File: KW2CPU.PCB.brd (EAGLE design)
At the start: 50 x 30 mm, 57 parts, among them IC1 AT45DB161D8S1

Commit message: Rotated board
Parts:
- added LED1: (no value), adafruit:CHIPLED_0805
- added SJ1: (no value), jumper:SJ
- moved U$4 40.8 mm to (-3.79, 6.27), turned to 180 degrees
- moved U$5 38.3 mm to (1.16, -13.1), turned to 180 degrees
- moved U$6 35.1 mm to (33.0, -0.76), turned to 270 degrees
- moved R2 33.9 mm to (27.7, -12.2), turned to 90 degrees
- moved U$12 32.9 mm to (31.8, -1.01)
- moved C$16 32.7 mm to (0.12, -5.87), turned to 180 degrees
- moved C$18 31.2 mm to (0.14, -3.28), turned to 180 degrees
- moved C$15 31.1 mm to (0.14, 2.07), turned to 180 degrees
- moved L$17 31.0 mm to (0.58, -4.54), turned to 90 degrees
- moved R3 30.9 mm to (22.9, -14.0), turned to 0 degrees
- moved C$13 30.7 mm to (0.14, -0.83), turned to 180 degrees
- moved R$19 30.0 mm to (2.33, -7.61), turned to 270 degrees
- moved L$14 29.9 mm to (0.58, 0.50), turned to 90 degrees
- moved IC2 29.6 mm to (27.1, 8.89), turned to 270 degrees
- moved C$20 29.3 mm to (2.09, -6.33), turned to 0 degrees
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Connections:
- net GND: now also R$23.P$2
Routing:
- net N$22: track 37.7 -> 6.80 mm, vias 1 -> 0
- net N$40: track 38.2 -> 54.4 mm
- net N$13: track 33.1 -> 46.6 mm
- net N$41: track 33.6 -> 44.4 mm
- net N$44: track 34.4 -> 45.2 mm
- net N$11: track 40.0 -> 50.1 mm
- net N$43: track 31.8 -> 40.2 mm
- net +3V3: track 65.0 -> 56.7 mm, vias 10 -> 12
- net N$42: track 38.6 -> 46.7 mm
- net N$10: track 34.5 -> 41.9 mm
- net N$12: track 38.9 -> 45.1 mm
- net N$14: track 36.5 -> 37.2 mm
- net GND: vias 83 -> 84

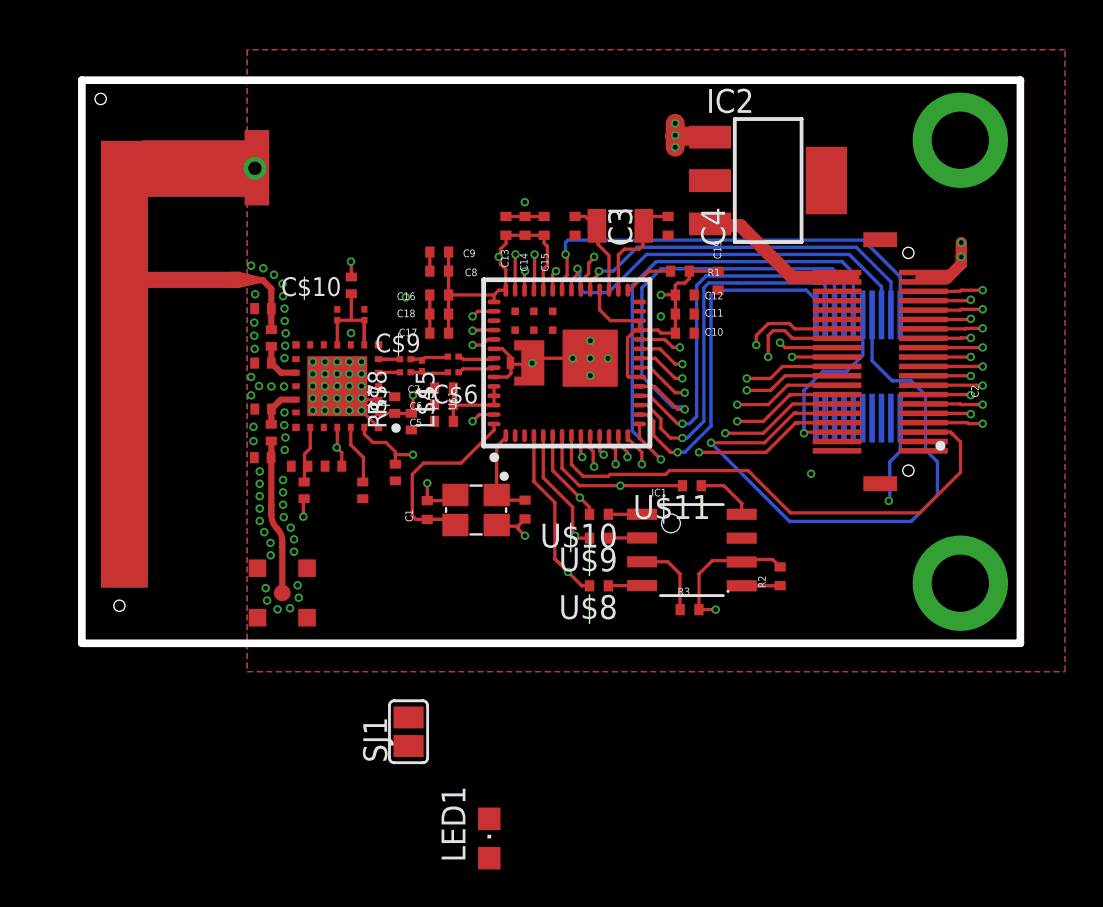
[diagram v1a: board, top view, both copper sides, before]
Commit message: Schematic fix
Almost done fixing schematic
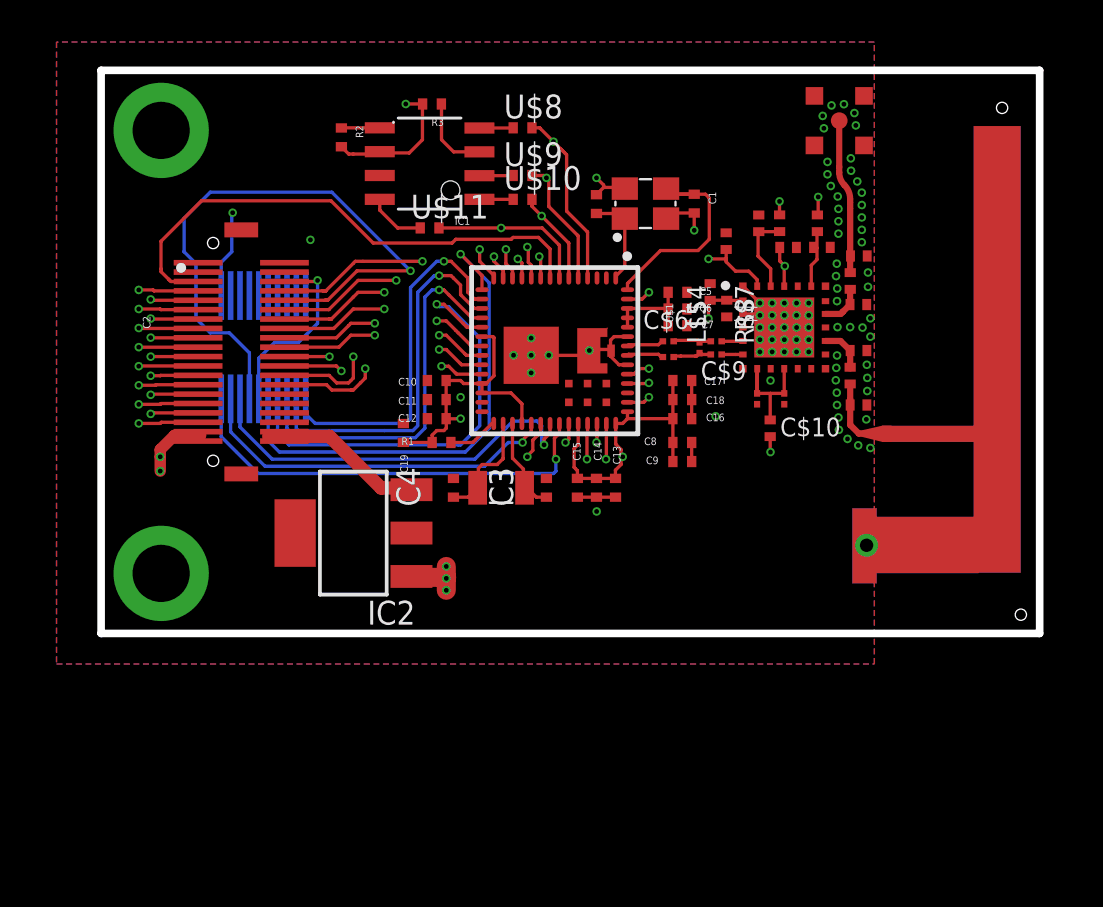
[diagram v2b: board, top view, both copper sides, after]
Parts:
- removed LED1: (no value), adafruit:CHIPLED_0805
- removed SJ1: (no value), jumper:SJ
- added R$2: (no value), GW-devices:RFMD0402
- moved U$4 41.8 mm to (35.8, -7.27), turned to 0 degrees
- moved U$5 38.9 mm to (30.8, 12.1), turned to 0 degrees
- moved U$6 34.0 mm to (-1.02, -0.24), turned to 90 degrees
- moved C$16 33.5 mm to (31.9, 4.87), turned to 0 degrees
- moved R2 33.1 mm to (4.31, 11.2), turned to 270 degrees
- moved C$18 32.2 mm to (31.9, 2.28), turned to 0 degrees
- moved C$15 32.1 mm to (31.9, -3.07), turned to 0 degrees
- moved L$17 31.9 mm to (31.4, 3.54), turned to 270 degrees
- moved C$13 31.7 mm to (31.9, -0.17), turned to 0 degrees
- moved U$12 31.7 mm to (0.16, 0.01), turned to 180 degrees
- moved L$14 30.9 mm to (31.4, -1.50), turned to 270 degrees
- moved R$19 30.8 mm to (29.7, 6.61), turned to 90 degrees
- moved R3 30.2 mm to (9.14, 13.0), turned to 180 degrees
- moved C$20 30.2 mm to (29.9, 5.33), turned to 180 degrees
- moved IC2 29.0 mm to (4.95, -9.89), turned to 90 degrees
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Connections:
- net +3V3: now also R$2.P$1
- net N$29: now also R$2.P$2
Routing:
- net N$29: track 3.20 -> 4.31 mm
- net +3V3: track 56.7 -> 57.5 mm, vias 12 -> 13

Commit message: Labeled all nets
Named nets and simplified JTAG adapter board.
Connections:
- net CLKM1 renamed XTAL_32M
- net CLKM2 renamed EXTAL_32M
- net N$1 renamed TAMPER/!RTC_WAKEUP
- net N$10 renamed PTA0/JTAG_TCLK/SWD_CLK/EZP_CLK/!UART0_CTS/!UART0_COL/FTM0_CH5
- net N$11 renamed PTA1/JTAG_TDI/EZP_DI/UART0/RX/FTM0_CH6
- net N$12 renamed PTA2/JTAG_TDO/TRACE?SWO/EZP_DO/UART0_TX/FTM0_CH7
- net N$13 renamed PTA3/JTAG_TMS/SWD_DIO/UART0_RTS/FTM0_CH0
- net N$14 renamed !RESET
- net N$15 renamed PTA4/LLWU_P3/!NMI!/!EZP_CS!/FTM0_CH1
- net N$16 renamed PTC5/LLWU_P8/SPI0_PCS0/UART1_TX/FTM0_CH3/CMP1_OUT
- net N$17 renamed PTC6/LLWU_P10/CMP0_IN0/SPI0_SOUT/PDB0_EXTRG/I2S0_RX_BCLK/I2S0_MCLK
- net N$18 renamed PTC7/CMP0_IN1/SPI0_SIN/USB_SOF_OUT/I2S0_RX_FS
- net N$19 renamed RFN
- net N$2 renamed RF_OUTP
- net N$20 renamed RFP
- net N$21 renamed ANT1
- net N$22 renamed VCC_DIG_PA
- net N$23 renamed F_ANT
- net N$24 renamed ANT2
- net N$25 renamed MMCX_ANT
- net N$26 renamed ANT_A
- net N$27 renamed ANTSEL
- net N$28 renamed EXTAL32
- net N$29 renamed C_LNA
- net N$3 renamed RF_OUTN
- net N$30 renamed RX_SWITCH
- net N$31 renamed TX_SWITCH
- net N$32 renamed XTAL32
- net N$33 renamed PTD2/LLWU_P13/SPI0_SOUT/UART2_RX/I2C0_SDA/GPIO4_BSM_DATA
- net N$34 renamed PTD1/ADC0_SE5B/SPI0_SCK/!UART2_CTS
- net N$35 renamed PTD3/SPI0_SIN/UART2_TX/I2C0_SCL/GPIO5_BSM_CLK
- net N$36 renamed PTD4/LLWU_P14/MADC0_SE21/SPI0_PCS1/!UART0_RTS!/FTM0_CH4/EWM_IN/GPIO_BSM_FRAME
- net N$37 renamed PTD5/ADC0_SE6B/SPI0_PCS2/!UART0_CTS!/!UART0_COL!/FTM0_CH5/!EWM_OUT
- net N$38 renamed PTD6/LLWU_P15/ADC0_SE7B/SPI0_PCS3/UART0_RX/FTM0_CH6/FTM0_FLT0
- net N$39 renamed PTD7/MADC0_SE22/CMT_IRO/UART0_TX/FTM0_CH7/FTM0_FLT1
- net N$40 renamed PTE0/MADC0_SE10/SPI1_PCS1/UART1_TX/MTRACE_CLKOUT/I2C1_SDA/RTC_CLKOUT
- net N$41 renamed PTE1/LLWU_P0/MADC0_SE11/SPI1_SOUT/UART1_RX/MTRACE_D3/I2C1_SCL/SPI1_SIN
- net N$42 renamed PTE2/LLWU_P1/MADC0_DP1/SPI1_SCK/!UART1_CTS!/MTRACE_D2
- net N$43 renamed PTE3/MADC0_DM1/SPI1_SIN/!UART1_RTS!/MTRACE_D1/SPI1_SOUT
- net N$44 renamed PTE4/LLWU_P2/SPI1_PCS0/MTRACE_D0
- net N$45 renamed PTE16/ADC0_SE4A/SPI0_PCS0/UART2_TX/FTM_CLKIN0/FTM0_FLT3
- net N$46 renamed PTE17/ADC0_SE5A/SPI0_SCK/UART2_RX/FTM_CLKIN1/LPTMR0_ALT3
- net N$47 renamed PTE18/ADC0_SE6A/SPI0_SOUT/!UART2_CTS!/I2C0_SDA
- net N$48 renamed PTE19/ADC0_SE7A/SPI0_SIN/!UART2_RTS!/I2C0_SCL
- net N$49 renamed PTA18/EXTAL0/FTM0_FTL2_FTM_CLKIN0
- net N$50 renamed PTA19/XTAL0/FTM1_FLT0/FTM_CLKIN1/LPTMR0_ALT1
- net N$51 renamed !CS
- net N$52 renamed SCK
- net N$53 renamed SI
- net N$7 renamed PTC4/LLWU_P8/SPI0_PCS0/UART1_TX/FTM0_CH3/CMP1_OUT

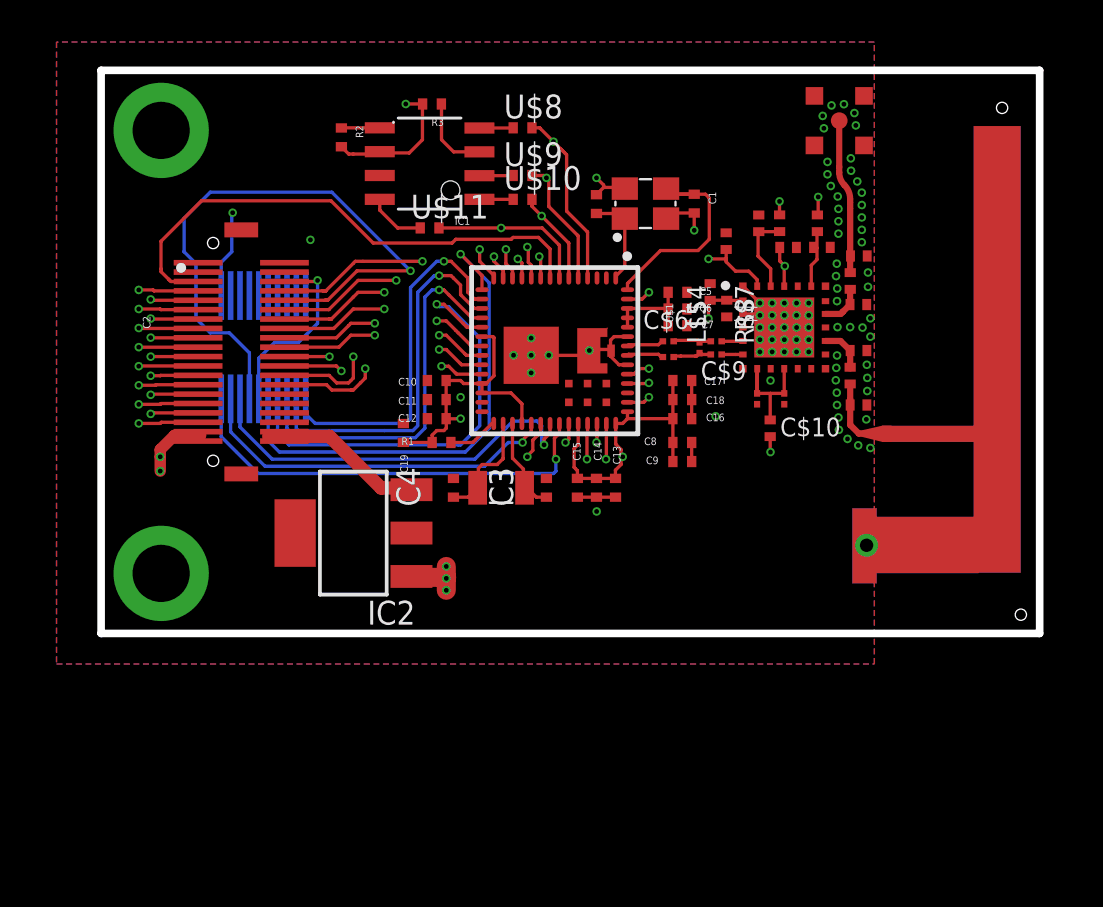
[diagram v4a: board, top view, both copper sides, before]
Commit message: Fixed RefDes, issues with names disappearing
Names on layout disappearing (for RF front end parts)
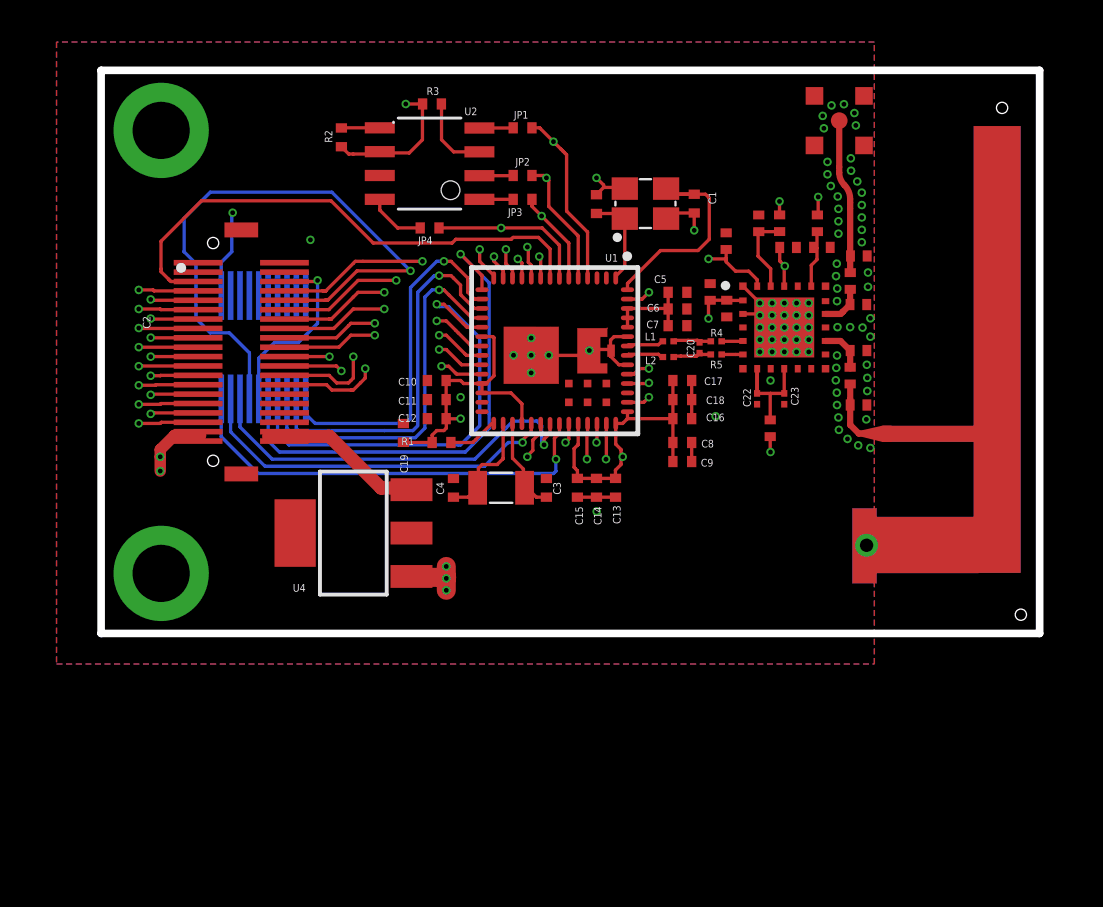
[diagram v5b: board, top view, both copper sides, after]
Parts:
- renumbered C$10 to C23, C$13 to C25, C$15 to C24, C$16 to C27, C$18 to C26, C$20 to C28, C$21 to C29, C$22 to C30, C$24 to C21, C$6 to C20, C$9 to C22, IC1 to U2, IC2 to U4, L$11 to L3, L$14 to L4, L$17 to L5, L$4 to L1, L$5 to L2, R$1 to R7, R$19 to R9, R$2 to R8, R$23 to R6, R$7 to R4, R$8 to R5, U$1 to U1, U$10 to JP3, U$11 to JP4, U$12 to J2, U$2 to X2, U$3 to U3, U$4 to U5, U$5 to J3, U$6 to J1, U$7 to X1, U$8 to JP1, U$9 to JP2

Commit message: Added test points
JTAG and front-end control test points
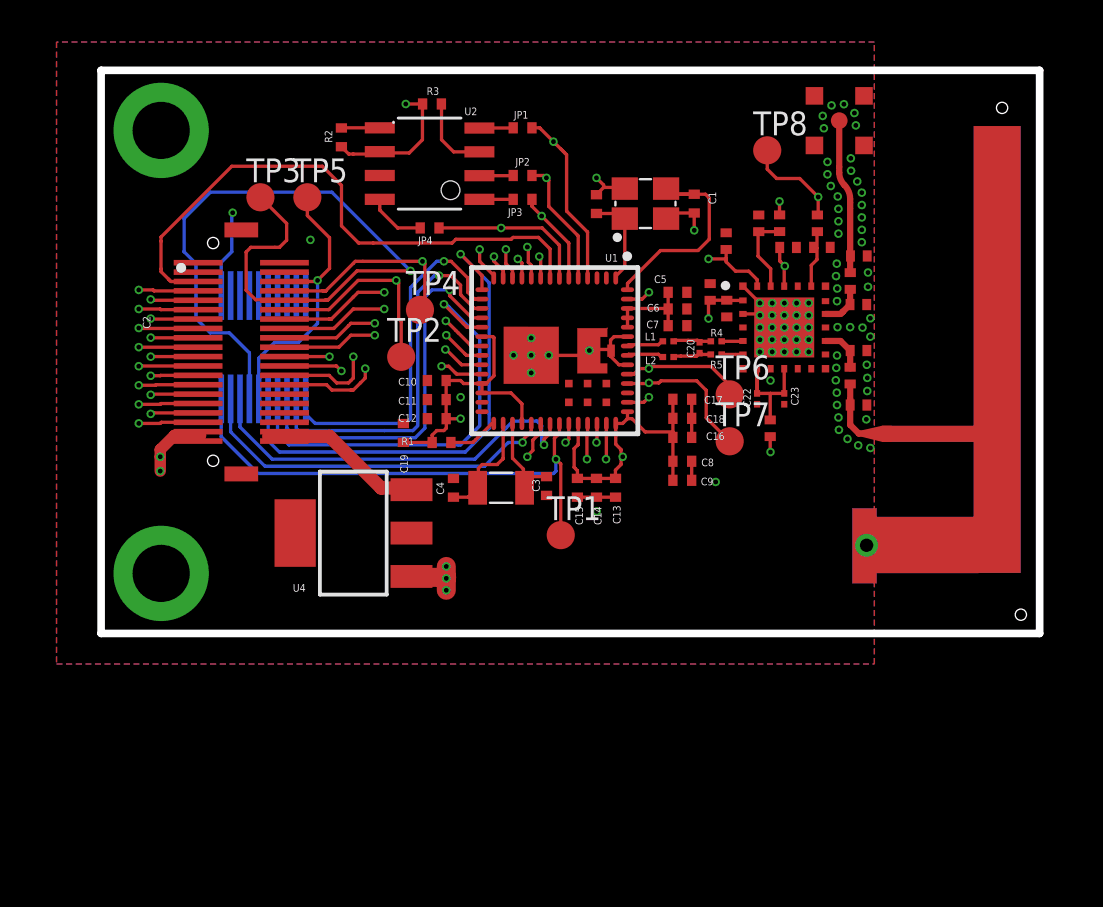
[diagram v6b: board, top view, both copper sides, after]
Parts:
- added TP1, TP2, TP3, TP4, TP5, TP6, TP7, TP8: PTR1TP15R, testpad:TP15R
- moved C17 1.00 mm to (22.5, -2.76)
- moved C18 1.00 mm to (22.5, -3.78)
- moved C8 1.00 mm to (22.5, -6.06)
- moved C9 1.00 mm to (22.5, -7.08)
- moved C16 1.00 mm to (22.5, -4.79)
- moved C3 0.10 mm to (15.2, -7.38), turned to 270 degrees
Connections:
- net !RESET: now also TP5.TP
- net ANT_A: now also TP8.TP
- net PTA0/JTAG_TCLK/SWD_CLK/EZP_CLK/!UART0_CTS/!UART0_COL/FTM0_CH5: now also TP4.TP
- net PTA1/JTAG_TDI/EZP_DI/UART0/RX/FTM0_CH6: now also TP3.TP
- net PTA2/JTAG_TDO/TRACE?SWO/EZP_DO/UART0_TX/FTM0_CH7: now also TP2.TP
- net PTA3/JTAG_TMS/SWD_DIO/UART0_RTS/FTM0_CH0: now also TP1.TP
- net RX_SWITCH: now also TP7.TP
- net TX_SWITCH: now also TP6.TP
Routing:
- net PTA1/JTAG_TDI/EZP_DI/UART0/RX/FTM0_CH6: track 50.1 -> 59.7 mm
- net RX_SWITCH: track 22.4 -> 28.9 mm
- net TX_SWITCH: track 16.8 -> 22.1 mm
- net !RESET: track 37.2 -> 42.4 mm
- net ANT_A: track 27.1 -> 31.4 mm
- net PTA2/JTAG_TDO/TRACE?SWO/EZP_DO/UART0_TX/FTM0_CH7: track 45.0 -> 49.2 mm
- net PTA3/JTAG_TMS/SWD_DIO/UART0_RTS/FTM0_CH0: track 46.6 -> 50.7 mm
- net PTA0/JTAG_TCLK/SWD_CLK/EZP_CLK/!UART0_CTS/!UART0_COL/FTM0_CH5: track 41.9 -> 45.3 mm
- net PTD1/ADC0_SE5B/SPI0_SCK/!UART2_CTS: track 29.5 -> 32.4 mm
- net PTE3/MADC0_DM1/SPI1_SIN/!UART1_RTS!/MTRACE_D1/SPI1_SOUT: track 40.2 -> 40.9 mm
